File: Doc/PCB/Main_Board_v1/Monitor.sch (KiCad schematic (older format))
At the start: 36 parts, among them J2 Conn_01x03_Male, J3 Valve connector, J4 UART, J5 I2C Interface LCD, J6 BUZZER, Q1 IRLZ34N, U1 7805, U2 LM358, U3 XPRESS-40

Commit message: New Schemartics. Clean up monitor
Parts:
- removed J2: Conn_01x03_Male, Connector_PinHeader_2.54mm:PinHeader_1x02_P2.54mm_Horizontal, symbol Connector:Conn_01x03_Male
- removed J3: Valve connector, symbol Connector:Screw_Terminal_01x02
- removed J6: BUZZER, Connector_PinHeader_2.54mm:PinHeader_1x02_P2.54mm_Horizontal, symbol Connector:Conn_01x02_Male
- removed J?: Power input 12V, symbol Connector:Screw_Terminal_01x02
- removed U1: 7805, Package_TO_SOT_THT:TO-220-3_Vertical, symbol Power_Management:7805
- removed U3: XPRESS-40, symbol MCU_Microchip_PIC18:XPRESS-40
- added C10, C20: 1uF, Capacitor_THT:C_Rect_L7.0mm_W2.5mm_P5.00mm, symbol Device:C
- added C12: 100nF, Capacitor_THT:C_Rect_L9.0mm_W3.3mm_P7.50mm_MKT, symbol Device:C
- added D4: 1N4007, Diode_THT:D_DO-41_SOD81_P10.16mm_Horizontal, symbol Diode:1N4001
- added J1, J2: TE_3.5mm_Screwless_P2, Ventilator:PinHeader_1x02_Screwless_3.5mm, symbol Ventilator:TE_3.5mm_Screwless_P2
- added J4: Conn_01x08, Connector_PinHeader_2.54mm:PinHeader_1x08_P2.54mm_Horizontal, symbol Connector_Generic:Conn_01x08
- added J5: Buzzer, Connector_PinHeader_2.54mm:PinHeader_1x02_P2.54mm_Vertical, symbol Connector_Generic:Conn_01x02
- added R1, R7: 470, Resistor_THT:R_Axial_DIN0207_L6.3mm_D2.5mm_P10.16mm_Horizontal, symbol Device:R
- added R24: 22k, Resistor_THT:R_Axial_DIN0207_L6.3mm_D2.5mm_P10.16mm_Horizontal, symbol Device:R
- added R25: 10k, Resistor_THT:R_Axial_DIN0207_L6.3mm_D2.5mm_P10.16mm_Horizontal, symbol Device:R
- added S1, S2: MPXV5004DP, Ventilator:1351-01, symbol Ventilator:MPXV5004DP
- added U2: LM7805_TO220, Package_TO_SOT_THT:TO-220-3_Vertical, symbol Regulator_Linear:LM7805_TO220
- added U3: XPRESS-40, Ventilator:EXPRESS-40_DIP_40, symbol Ventilator:XPRESS-40
- J3: renamed from J4; value UART -> UART_M; footprint Connector_PinHeader_2.54mm:PinHeader_1x03_P2.54mm_Horizontal -> Connector_PinHeader_2.54mm:PinHeader_1x03_P2.54mm_Vertical
- J6: renamed from J5; value I2C Interface LCD -> I2C Interface LCD_M; footprint Connector_PinHeader_2.54mm:PinHeader_1x04_P2.54mm_Horizontal -> Connector_PinHeader_2.54mm:PinHeader_1x04_P2.54mm_Vertical
- MK1: footprint (none) -> Connector_PinHeader_2.54mm:PinHeader_1x02_P2.54mm_Vertical
- U1: renamed from U2; footprint Package_DIP:DIP-8-16_W7.62mm -> Package_DIP:DIP-8_W7.62mm_LongPads
- renumbered C6 to C1, C10 to C11, C11 to C13, C3 to C2, C7 to C3, C8 to C4, C1 to C5, C2 to C6, C4 to C7, C5 to C8, R7 to R10, R10 to R11, R8 to R12, R1 to R6, R6 to R8
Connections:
- net labels added: +12V_M, +5V_M, ALARM_HISTORY, ALARM_LED, ALARM_MUTE, BUZZER, ICSPCLK_M, ICSPDAT_M, LCD_SCL_M, LCD_SDA_M, MEAS_12V, MIC, PROG_CONN, PTR2, PTR4, RX, SV1, TX, nMCLR
- net labels removed: +12V, +5V
- wire segments 151 -> 193
- no-connect marks 20 -> 22
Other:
- moved on the sheet: C1, C13, C2, C3, C4, C5, C6, C7, C8, D1, J3, J6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

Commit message: First layout of Monitor
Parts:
- removed TP1: ALARM LED, Connector_PinHeader_2.54mm:PinHeader_1x02_P2.54mm_Vertical, symbol Connector:TestPoint_2Pole
- removed TP2: ALARM MUTE, Connector_PinHeader_2.54mm:PinHeader_1x02_P2.54mm_Vertical, symbol Connector:TestPoint_2Pole
- removed TP3: ALARM HISTORY, Connector_PinHeader_2.54mm:PinHeader_1x02_P2.54mm_Vertical, symbol Connector:TestPoint_2Pole
- added J14: MUTE+LED, Ventilator:PH_4_pol, symbol Connector_Generic:Conn_01x04
- added J15: HISTORY, Ventilator:PH_2_pol, symbol Connector_Generic:Conn_01x02
- J5: value Buzzer -> BUZZER; footprint Connector_PinHeader_2.54mm:PinHeader_1x02_P2.54mm_Vertical -> Ventilator:PH_2_pol
- J6: footprint Connector_PinHeader_2.54mm:PinHeader_1x04_P2.54mm_Vertical -> Ventilator:PH_4_pol
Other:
- moved on the sheet: J5, R12
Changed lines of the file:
@@
 Text GLabel 7300 2100 2    50   BiDi ~ 0
 SDA
-$Comp
-L power:GND #PWR?
-U 1 1 5EB072C9
-P 11000 3450
-AR Path="/5EB072C9" Ref="#PWR?"  Part="1"
-AR Path="/5EA602EB/5EB072C9" Ref="#PWR?"  Part="1"
-AR Path="/5E9337AC/5EB072C9" Ref="#PWR040"  Part="1"
-F 0 "#PWR040" H 11000 3200 50  0001 C CNN
-F 1 "GND" H 11005 3277 50  0000 C CNN
-F 2 "" H 11000 3450 50  0001 C CNN
-F 3 "" H 11000 3450 50  0001 C CNN
-	1    11000 3450
-	1    0    0    -1
-$EndComp
-Wire Wire Line
-	10800 2600 11000 2600
 Wire Wire Line
 	1750 3750 1750 3900
@@
 	9300 3200 9550 3200
 Wire Wire Line
-	11000 2600 11000 2900
-Wire Wire Line
-	10800 3200 11000 3200
-Connection ~ 11000 3200
-Wire Wire Line
-	10800 2900 11000 2900
-Connection ~ 11000 2900
-Wire Wire Line
-	11000 2900 11000 3200
-Wire Wire Line
 	9800 2500 9800 2900
 Connection ~ 9800 2900
 Wire Wire Line
-	9800 2900 10400 2900
-Wire Wire Line
 	9550 2500 9550 3200
 Connection ~ 9550 3200
 Wire Wire Line
-	9550 3200 10400 3200
-Wire Wire Line
 	9550 2000 9800 2000
 Wire Wire Line
@@
 	6450 2800 9300 2800
 Wire Wire Line
-	9300 2800 9300 2600
-Wire Wire Line
-	9300 2600 9950 2600
+	9300 2800 9300 2700
+Wire Wire Line
+	9300 2700 9950 2700
 Wire Wire Line
 	6450 2900 9800 2900
@@
 	6450 2700 6900 2700
 Wire Wire Line
-	10250 2600 10400 2600
-Wire Wire Line
-	11000 3200 11000 3450
-Wire Wire Line
-	10250 3550 10300 3550
+	10250 3550 10500 3550
 Wire Wire Line
 	10250 3650 10250 3550
@@
 	9100 3100 9100 3450
 Wire Wire Line
-	9100 3450 10300 3450
+	9100 3450 10500 3450
 Wire Wire Line
 	2100 5950 1850 5950
@@
 F 0 "J6" H 10722 1082 50  0000 R CNN
 F 1 "I2C Interface LCD_M" H 11051 856 50  0000 R CNN
-F 2 "Connector_PinHeader_2.54mm:PinHeader_1x04_P2.54mm_Vertical" H 10750 1200 50  0001 C CNN
+F 2 "Ventilator:PH_4_pol" H 10750 1200 50  0001 C CNN
 F 3 "~" H 10750 1200 50  0001 C CNN
 	1    10750 1200
@@
 $EndComp
 $Comp
-L Connector:TestPoint_2Pole TP?
-U 1 1 5EB07324
-P 10600 3200
-AR Path="/5EB07324" Ref="TP?"  Part="1"
-AR Path="/5EA602EB/5EB07324" Ref="TP?"  Part="1"
-AR Path="/5E9337AC/5EB07324" Ref="TP3"  Part="1"
-F 0 "TP3" H 10600 3395 50  0000 C CNN
-F 1 "ALARM HISTORY" H 10600 3304 50  0000 C CNN
-F 2 "Connector_PinHeader_2.54mm:PinHeader_1x02_P2.54mm_Vertical" H 10600 3200 50  0001 C CNN
-F 3 "~" H 10600 3200 50  0001 C CNN
-	1    10600 3200
-	1    0    0    -1
-$EndComp
-$Comp
-L Connector:TestPoint_2Pole TP?
-U 1 1 5EB0731E
-P 10600 2900
-AR Path="/5EB0731E" Ref="TP?"  Part="1"
-AR Path="/5EA602EB/5EB0731E" Ref="TP?"  Part="1"
-AR Path="/5E9337AC/5EB0731E" Ref="TP2"  Part="1"
-F 0 "TP2" H 10600 3095 50  0000 C CNN
-F 1 "ALARM MUTE" H 10600 3004 50  0000 C CNN
-F 2 "Connector_PinHeader_2.54mm:PinHeader_1x02_P2.54mm_Vertical" H 10600 2900 50  0001 C CNN
-F 3 "~" H 10600 2900 50  0001 C CNN
-	1    10600 2900
-	1    0    0    -1
-$EndComp
-$Comp
 L Diode:1N4001 D?
 U 1 1 5EB072D6
@@
 $EndComp
 $Comp
-L Connector:TestPoint_2Pole TP?
-U 1 1 5EB072C3
-P 10600 2600
-AR Path="/5EB072C3" Ref="TP?"  Part="1"
-AR Path="/5EA602EB/5EB072C3" Ref="TP?"  Part="1"
-AR Path="/5E9337AC/5EB072C3" Ref="TP1"  Part="1"
-F 0 "TP1" H 10600 2795 50  0000 C CNN
-F 1 "ALARM LED" H 10600 2704 50  0000 C CNN
-F 2 "Connector_PinHeader_2.54mm:PinHeader_1x02_P2.54mm_Vertical" H 10600 2600 50  0001 C CNN
-F 3 "~" H 10600 2600 50  0001 C CNN
-	1    10600 2600
-	1    0    0    -1
-$EndComp
-$Comp
 L Device:R R?
 U 1 1 5EB072BC
-P 10100 2600
+P 10100 2700
 AR Path="/5EB072BC" Ref="R?"  Part="1"
 AR Path="/5EA602EB/5EB072BC" Ref="R?"  Part="1"
 AR Path="/5E9337AC/5EB072BC" Ref="R12"  Part="1"
-F 0 "R12" V 9893 2600 50  0000 C CNN
-F 1 "470" V 9984 2600 50  0000 C CNN
-F 2 "Resistor_THT:R_Axial_DIN0207_L6.3mm_D2.5mm_P10.16mm_Horizontal" V 10030 2600 50  0001 C CNN
-F 3 "~" H 10100 2600 50  0001 C CNN
-	1    10100 2600
+F 0 "R12" V 9893 2700 50  0000 C CNN
+F 1 "470" V 9984 2700 50  0000 C CNN
+F 2 "Resistor_THT:R_Axial_DIN0207_L6.3mm_D2.5mm_P10.16mm_Horizontal" V 10030 2700 50  0001 C CNN
+F 3 "~" H 10100 2700 50  0001 C CNN
+	1    10100 2700
 	0    1    1    0
 $EndComp
@@
 L Connector_Generic:Conn_01x02 J5
 U 1 1 5F29E587
-P 10500 3450
-F 0 "J5" H 10580 3442 50  0000 L CNN
-F 1 "Buzzer" H 10580 3351 50  0000 L CNN
-F 2 "Connector_PinHeader_2.54mm:PinHeader_1x02_P2.54mm_Vertical" H 10500 3450 50  0001 C CNN
-F 3 "~" H 10500 3450 50  0001 C CNN
-	1    10500 3450
+P 10700 3450
+F 0 "J5" H 10780 3442 50  0000 L CNN
+F 1 "BUZZER" H 10780 3351 50  0000 L CNN
+F 2 "Ventilator:PH_2_pol" H 10700 3450 50  0001 C CNN
+F 3 "~" H 10700 3450 50  0001 C CNN
+	1    10700 3450
 	1    0    0    -1
 $EndComp
@@
 Wire Wire Line
 	2950 3150 2950 3200
+$Comp
+L Connector_Generic:Conn_01x04 J14
+U 1 1 5E9D817B
+P 10700 2800
+F 0 "J14" H 10780 2792 50  0000 L CNN
+F 1 "MUTE+LED" H 10780 2701 50  0000 L CNN
+F 2 "Ventilator:PH_4_pol" H 10700 2800 50  0001 C CNN
+F 3 "~" H 10700 2800 50  0001 C CNN
+	1    10700 2800
+	1    0    0    -1
+$EndComp
+Wire Wire Line
+	10250 2700 10500 2700
+Wire Wire Line
+	10500 2800 10250 2800
+Wire Wire Line
+	9800 2900 10500 2900
+$Comp
+L Connector_Generic:Conn_01x02 J15
+U 1 1 5EA6CD7A
+P 10700 3200
+F 0 "J15" H 10780 3192 50  0000 L CNN
+F 1 "HISTORY" H 10780 3101 50  0000 L CNN
+F 2 "Ventilator:PH_2_pol" H 10700 3200 50  0001 C CNN
+F 3 "~" H 10700 3200 50  0001 C CNN
+	1    10700 3200
+	1    0    0    -1
+$EndComp
+Wire Wire Line
+	9550 3200 10500 3200
+Wire Wire Line
+	10250 2800 10250 3000
+Connection ~ 10250 3550
+Wire Wire Line
+	10500 3300 10250 3300
+Connection ~ 10250 3300
+Wire Wire Line
+	10250 3300 10250 3550
+Wire Wire Line
+	10500 3000 10250 3000
+Connection ~ 10250 3000
+Wire Wire Line
+	10250 3000 10250 3300
 $EndSCHEMATC

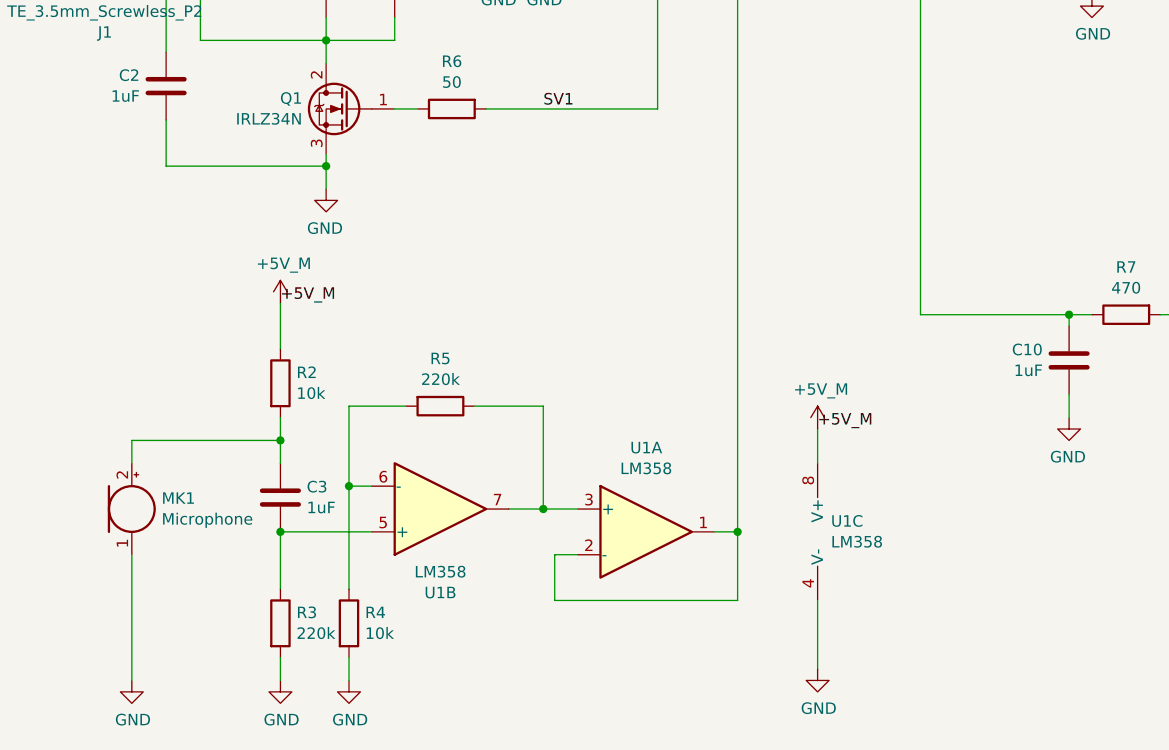
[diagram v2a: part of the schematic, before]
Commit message: Updated Monitor Schematic
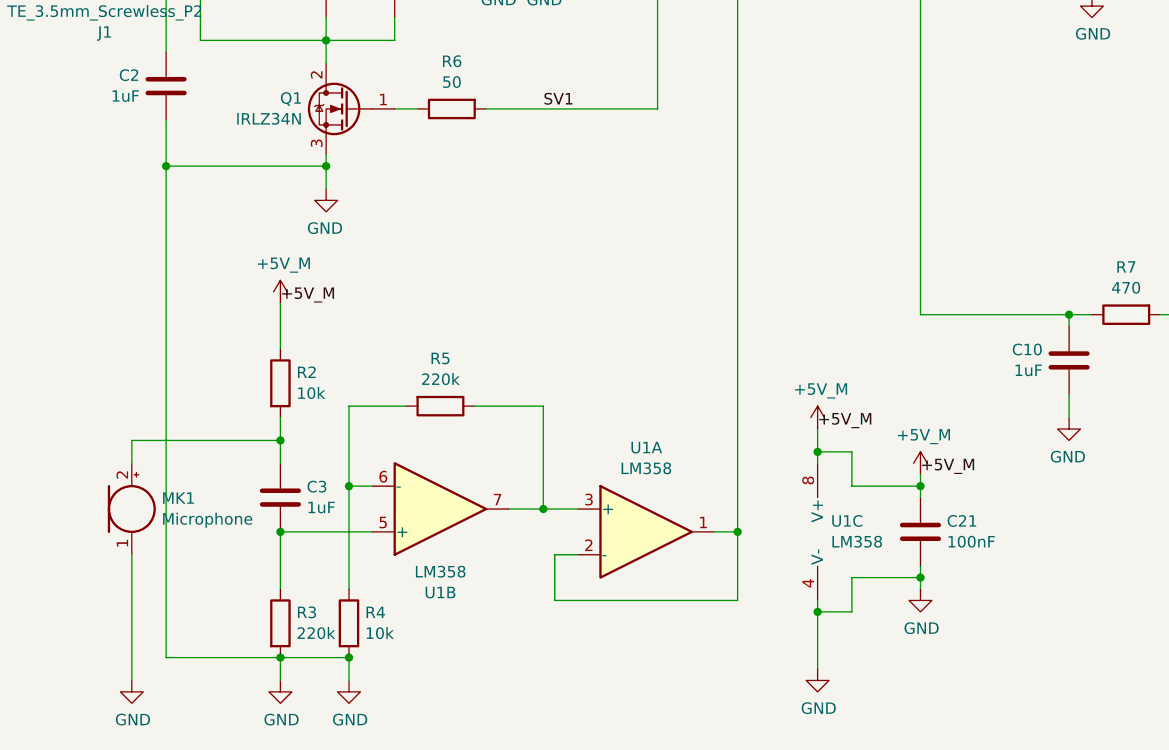
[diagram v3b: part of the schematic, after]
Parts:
- added C21: 100nF, Capacitor_THT:C_Rect_L9.0mm_W3.3mm_P7.50mm_MKT, symbol Device:C
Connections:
- wire segments 193 -> 208
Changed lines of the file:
@@
 $EndComp
 Wire Wire Line
-	3900 6050 3900 6200
-Wire Wire Line
-	3900 6800 3900 7100
+	3900 6050 3900 6150
+Wire Wire Line
+	3900 6800 3900 6850
 Connection ~ 3550 6500
 NoConn ~ 6450 3700
@@
 Wire Wire Line
 	1050 3900 1000 3900
-Wire Wire Line
-	1050 4700 1050 4900
 Wire Wire Line
 	1050 4900 1750 4900
@@
 Wire Wire Line
 	10250 3000 10250 3300
+Wire Wire Line
+	1050 4700 1050 4900
+Connection ~ 1550 7050
+Wire Wire Line
+	1550 7050 1050 7050
+Connection ~ 1850 7050
+Wire Wire Line
+	1850 7050 1550 7050
+Connection ~ 1050 4900
+Wire Wire Line
+	1050 4900 1050 7050
+$Comp
+L power:GND #PWR?
+U 1 1 5EADB5B4
+P 4350 6750
+AR Path="/5EADB5B4" Ref="#PWR?"  Part="1"
+AR Path="/5EA602EB/5EADB5B4" Ref="#PWR?"  Part="1"
+AR Path="/5E9337AC/5EADB5B4" Ref="#PWR08"  Part="1"
+F 0 "#PWR08" H 4350 6500 50  0001 C CNN
+F 1 "GND" H 4355 6577 50  0000 C CNN
+F 2 "" H 4350 6750 50  0001 C CNN
+F 3 "" H 4350 6750 50  0001 C CNN
+	1    4350 6750
+	1    0    0    -1
+$EndComp
+Wire Wire Line
+	4350 6650 4350 6700
+Wire Wire Line
+	4350 6250 4350 6300
+Wire Wire Line
+	4050 6300 4350 6300
+Connection ~ 4350 6300
+Wire Wire Line
+	4350 6300 4350 6350
+Wire Wire Line
+	4050 6700 4350 6700
+Connection ~ 4350 6700
+Wire Wire Line
+	4350 6700 4350 6750
+$Comp
+L Device:C C?
+U 1 1 5EADB5C2
+P 4350 6500
+AR Path="/5EADB5C2" Ref="C?"  Part="1"
+AR Path="/5EA602EB/5EADB5C2" Ref="C?"  Part="1"
+AR Path="/5E9337AC/5EADB5C2" Ref="C21"  Part="1"
+F 0 "C21" H 4465 6546 50  0000 L CNN
+F 1 "100nF" H 4465 6455 50  0000 L CNN
+F 2 "Capacitor_THT:C_Rect_L9.0mm_W3.3mm_P7.50mm_MKT" H 4388 6350 50  0001 C CNN
+F 3 "~" H 4350 6500 50  0001 C CNN
+	1    4350 6500
+	1    0    0    -1
+$EndComp
+Text Label 4350 6250 0    50   ~ 0
++5V_M
+$Comp
+L Ventilator:+5V_M #PWR05
+U 1 1 5EADB5C9
+P 4350 6250
+F 0 "#PWR05" H 4350 6100 50  0001 C CNN
+F 1 "+5V_M" H 4365 6423 50  0000 C CNN
+F 2 "" H 4350 6250 50  0001 C CNN
+F 3 "" H 4350 6250 50  0001 C CNN
+	1    4350 6250
+	1    0    0    -1
+$EndComp
+Wire Wire Line
+	3900 6150 4050 6150
+Wire Wire Line
+	4050 6150 4050 6300
+Connection ~ 3900 6150
+Wire Wire Line
+	3900 6150 3900 6200
+Wire Wire Line
+	4050 6700 4050 6850
+Wire Wire Line
+	4050 6850 3900 6850
+Connection ~ 3900 6850
+Wire Wire Line
+	3900 6850 3900 7100
 $EndSCHEMATC

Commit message: Update in the PCB design. New docs and images
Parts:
- removed J14: MUTE+LED, Ventilator:PH_4_pol, symbol Connector_Generic:Conn_01x04
- removed J15: HISTORY, Ventilator:PH_2_pol, symbol Connector_Generic:Conn_01x02
- added J14: Button_LED, Ventilator:PushButton_LED, symbol Ventilator:Button_LED
- added J15: Button, Ventilator:PushButton, symbol Ventilator:Button
- added TP1, TP2, TP3, TP4: TestPoint, Ventilator:LCD_DRILL, symbol Connector:TestPoint
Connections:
- wire segments 208 -> 212
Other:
- moved on the sheet: J5, R12
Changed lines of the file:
@@
 	1750 4350 1750 4450
-Wire Wire Line
-	9300 3000 9300 3200
-Wire Wire Line
-	9300 3200 9550 3200
 Wire Wire Line
 	9800 2500 9800 2900
 Connection ~ 9800 2900
 Wire Wire Line
-	9550 2500 9550 3200
-Connection ~ 9550 3200
-Wire Wire Line
 	9550 2000 9800 2000
 Wire Wire Line
@@
 	9550 2200 9550 2000
 Connection ~ 9550 2000
-Wire Wire Line
-	6450 2800 9300 2800
-Wire Wire Line
-	9300 2800 9300 2700
-Wire Wire Line
-	9300 2700 9950 2700
 Wire Wire Line
 	6450 2900 9800 2900
@@
 	6450 2700 6900 2700
 Wire Wire Line
-	10250 3550 10500 3550
-Wire Wire Line
-	10250 3650 10250 3550
+	10250 3750 10500 3750
+Wire Wire Line
+	10250 3850 10250 3750
 $Comp
 L power:GND #PWR?
 U 1 1 5EB07248
-P 10250 3650
+P 10250 3850
 AR Path="/5EB07248" Ref="#PWR?"  Part="1"
 AR Path="/5EA602EB/5EB07248" Ref="#PWR?"  Part="1"
 AR Path="/5E9337AC/5EB07248" Ref="#PWR035"  Part="1"
-F 0 "#PWR035" H 10250 3400 50  0001 C CNN
-F 1 "GND" H 10255 3477 50  0000 C CNN
-F 2 "" H 10250 3650 50  0001 C CNN
-F 3 "" H 10250 3650 50  0001 C CNN
-	1    10250 3650
+F 0 "#PWR035" H 10250 3600 50  0001 C CNN
+F 1 "GND" H 10255 3677 50  0000 C CNN
+F 2 "" H 10250 3850 50  0001 C CNN
+F 3 "" H 10250 3850 50  0001 C CNN
+	1    10250 3850
 	-1   0    0    -1
 $EndComp
 Wire Wire Line
-	6450 3100 9100 3100
-Wire Wire Line
-	9100 3100 9100 3450
-Wire Wire Line
-	9100 3450 10500 3450
+	9100 3650 10500 3650
 Wire Wire Line
 	2100 5950 1850 5950
@@
 L Device:R R?
 U 1 1 5EB072BC
-P 10100 2700
+P 10000 2800
 AR Path="/5EB072BC" Ref="R?"  Part="1"
 AR Path="/5EA602EB/5EB072BC" Ref="R?"  Part="1"
 AR Path="/5E9337AC/5EB072BC" Ref="R12"  Part="1"
-F 0 "R12" V 9893 2700 50  0000 C CNN
-F 1 "470" V 9984 2700 50  0000 C CNN
-F 2 "Resistor_THT:R_Axial_DIN0207_L6.3mm_D2.5mm_P10.16mm_Horizontal" V 10030 2700 50  0001 C CNN
-F 3 "~" H 10100 2700 50  0001 C CNN
-	1    10100 2700
+F 0 "R12" V 9793 2800 50  0000 C CNN
+F 1 "470" V 9884 2800 50  0000 C CNN
+F 2 "Resistor_THT:R_Axial_DIN0207_L6.3mm_D2.5mm_P10.16mm_Horizontal" V 9930 2800 50  0001 C CNN
+F 3 "~" H 10000 2800 50  0001 C CNN
+	1    10000 2800
 	0    1    1    0
 $EndComp
@@
 L Connector_Generic:Conn_01x02 J5
 U 1 1 5F29E587
-P 10700 3450
-F 0 "J5" H 10780 3442 50  0000 L CNN
-F 1 "BUZZER" H 10780 3351 50  0000 L CNN
-F 2 "Ventilator:PH_2_pol" H 10700 3450 50  0001 C CNN
-F 3 "~" H 10700 3450 50  0001 C CNN
-	1    10700 3450
+P 10700 3650
+F 0 "J5" H 10780 3642 50  0000 L CNN
+F 1 "BUZZER" H 10780 3551 50  0000 L CNN
+F 2 "Ventilator:PH_2_pol" H 10700 3650 50  0001 C CNN
+F 3 "~" H 10700 3650 50  0001 C CNN
+	1    10700 3650
 	1    0    0    -1
 $EndComp
@@
 Wire Wire Line
 	2950 3150 2950 3200
-$Comp
-L Connector_Generic:Conn_01x04 J14
-U 1 1 5E9D817B
-P 10700 2800
-F 0 "J14" H 10780 2792 50  0000 L CNN
-F 1 "MUTE+LED" H 10780 2701 50  0000 L CNN
-F 2 "Ventilator:PH_4_pol" H 10700 2800 50  0001 C CNN
-F 3 "~" H 10700 2800 50  0001 C CNN
-	1    10700 2800
-	1    0    0    -1
-$EndComp
-Wire Wire Line
-	10250 2700 10500 2700
-Wire Wire Line
-	10500 2800 10250 2800
 Wire Wire Line
 	9800 2900 10500 2900
-$Comp
-L Connector_Generic:Conn_01x02 J15
-U 1 1 5EA6CD7A
-P 10700 3200
-F 0 "J15" H 10780 3192 50  0000 L CNN
-F 1 "HISTORY" H 10780 3101 50  0000 L CNN
-F 2 "Ventilator:PH_2_pol" H 10700 3200 50  0001 C CNN
-F 3 "~" H 10700 3200 50  0001 C CNN
-	1    10700 3200
-	1    0    0    -1
-$EndComp
-Wire Wire Line
-	9550 3200 10500 3200
-Wire Wire Line
-	10250 2800 10250 3000
-Connection ~ 10250 3550
-Wire Wire Line
-	10500 3300 10250 3300
-Connection ~ 10250 3300
-Wire Wire Line
-	10250 3300 10250 3550
+Connection ~ 10250 3750
 Wire Wire Line
 	10500 3000 10250 3000
-Connection ~ 10250 3000
-Wire Wire Line
-	10250 3000 10250 3300
+Wire Wire Line
+	10250 3000 10250 3100
 Wire Wire Line
 	1050 4700 1050 4900
-Connection ~ 1550 7050
-Wire Wire Line
-	1550 7050 1050 7050
-Connection ~ 1850 7050
-Wire Wire Line
-	1850 7050 1550 7050
-Connection ~ 1050 4900
-Wire Wire Line
-	1050 4900 1050 7050
 $Comp
 L power:GND #PWR?
@@
 Wire Wire Line
 	3900 6850 3900 7100
+Wire Wire Line
+	6450 2800 9850 2800
+Wire Wire Line
+	10150 2800 10500 2800
+$Comp
+L Ventilator:Button_LED J14
+U 1 1 5EA7097A
+P 10550 2950
+F 0 "J14" H 10878 3001 50  0000 L CNN
+F 1 "Button_LED" H 10878 2910 50  0000 L CNN
+F 2 "Ventilator:PushButton_LED" H 10550 2950 50  0001 C CNN
+F 3 "" H 10550 2950 50  0001 C CNN
+	1    10550 2950
+	1    0    0    -1
+$EndComp
+Wire Wire Line
+	10500 3100 10250 3100
+Connection ~ 10250 3100
+Wire Wire Line
+	6450 3100 9100 3100
+Wire Wire Line
+	9100 3100 9100 3650
+$Comp
+L Ventilator:Button J15
+U 1 1 5EADEC62
+P 10550 3350
+F 0 "J15" H 10878 3396 50  0000 L CNN
+F 1 "Button" H 10878 3305 50  0000 L CNN
+F 2 "Ventilator:PushButton" H 10550 3350 50  0001 C CNN
+F 3 "" H 10550 3350 50  0001 C CNN
+	1    10550 3350
+	1    0    0    -1
+$EndComp
+Wire Wire Line
+	10250 3100 10250 3400
+Wire Wire Line
+	9300 3300 9550 3300
+Wire Wire Line
+	9300 3000 9300 3300
+Wire Wire Line
+	9550 2500 9550 3300
+Connection ~ 9550 3300
+Wire Wire Line
+	9550 3300 10500 3300
+Wire Wire Line
+	10500 3400 10250 3400
+Connection ~ 10250 3400
+Wire Wire Line
+	10250 3400 10250 3750
+$Comp
+L Connector:TestPoint TP3
+U 1 1 5EB96CC6
+P 9050 4850
+F 0 "TP3" H 9108 4968 50  0000 L CNN
+F 1 "TestPoint" H 9108 4877 50  0000 L CNN
+F 2 "Ventilator:LCD_DRILL" H 9250 4850 50  0001 C CNN
+F 3 "~" H 9250 4850 50  0001 C CNN
+	1    9050 4850
+	1    0    0    -1
+$EndComp
+$Comp
+L Connector:TestPoint TP2
+U 1 1 5EB97C9D
+P 8600 4850
+F 0 "TP2" H 8658 4968 50  0000 L CNN
+F 1 "TestPoint" H 8658 4877 50  0000 L CNN
+F 2 "Ventilator:LCD_DRILL" H 8800 4850 50  0001 C CNN
+F 3 "~" H 8800 4850 50  0001 C CNN
+	1    8600 4850
+	1    0    0    -1
+$EndComp
+$Comp
+L Connector:TestPoint TP1
+U 1 1 5EB98962
+P 8150 4850
+F 0 "TP1" H 8208 4968 50  0000 L CNN
+F 1 "TestPoint" H 8208 4877 50  0000 L CNN
+F 2 "Ventilator:LCD_DRILL" H 8350 4850 50  0001 C CNN
+F 3 "~" H 8350 4850 50  0001 C CNN
+	1    8150 4850
+	1    0    0    -1
+$EndComp
+$Comp
+L Connector:TestPoint TP4
+U 1 1 5EB99648
+P 9500 4850
+F 0 "TP4" H 9558 4968 50  0000 L CNN
+F 1 "TestPoint" H 9558 4877 50  0000 L CNN
+F 2 "Ventilator:LCD_DRILL" H 9700 4850 50  0001 C CNN
+F 3 "~" H 9700 4850 50  0001 C CNN
+	1    9500 4850
+	1    0    0    -1
+$EndComp
+$Comp
+L power:GND #PWR?
+U 1 1 5EB99F9D
+P 8900 5250
+AR Path="/5EB99F9D" Ref="#PWR?"  Part="1"
+AR Path="/5EA602EB/5EB99F9D" Ref="#PWR?"  Part="1"
+AR Path="/5E9337AC/5EB99F9D" Ref="#PWR012"  Part="1"
+F 0 "#PWR012" H 8900 5000 50  0001 C CNN
+F 1 "GND" H 8905 5077 50  0000 C CNN
+F 2 "" H 8900 5250 50  0001 C CNN
+F 3 "" H 8900 5250 50  0001 C CNN
+	1    8900 5250
+	1    0    0    -1
+$EndComp
+Wire Wire Line
+	8150 4850 8150 5100
+Wire Wire Line
+	8150 5100 8600 5100
+Wire Wire Line
+	8900 5100 8900 5250
+Wire Wire Line
+	9500 5100 9050 5100
+Wire Wire Line
+	9500 4850 9500 5100
+Connection ~ 8900 5100
+Wire Wire Line
+	9050 4850 9050 5100
+Connection ~ 9050 5100
+Wire Wire Line
+	9050 5100 8900 5100
+Wire Wire Line
+	8600 4850 8600 5100
+Connection ~ 8600 5100
+Wire Wire Line
+	8600 5100 8900 5100
 $EndSCHEMATC
